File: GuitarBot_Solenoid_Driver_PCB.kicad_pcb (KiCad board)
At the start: 2 copper layers, 123.2 x 109.2 mm, 89 parts, among them J3V3 Screw_Terminal_01x02, Q1 NMOS, Q10 NMOS, Q11 NMOS, Q12 NMOS, Q13 NMOS, Q14 NMOS, Q15 NMOS, Q16 NMOS, Q2 NMOS, Q3 NMOS, Q4 NMOS, Q5 NMOS, Q6 NMOS, Q7 NMOS, Q8 NMOS, Q9 NMOS, U1 MCP23017_SP

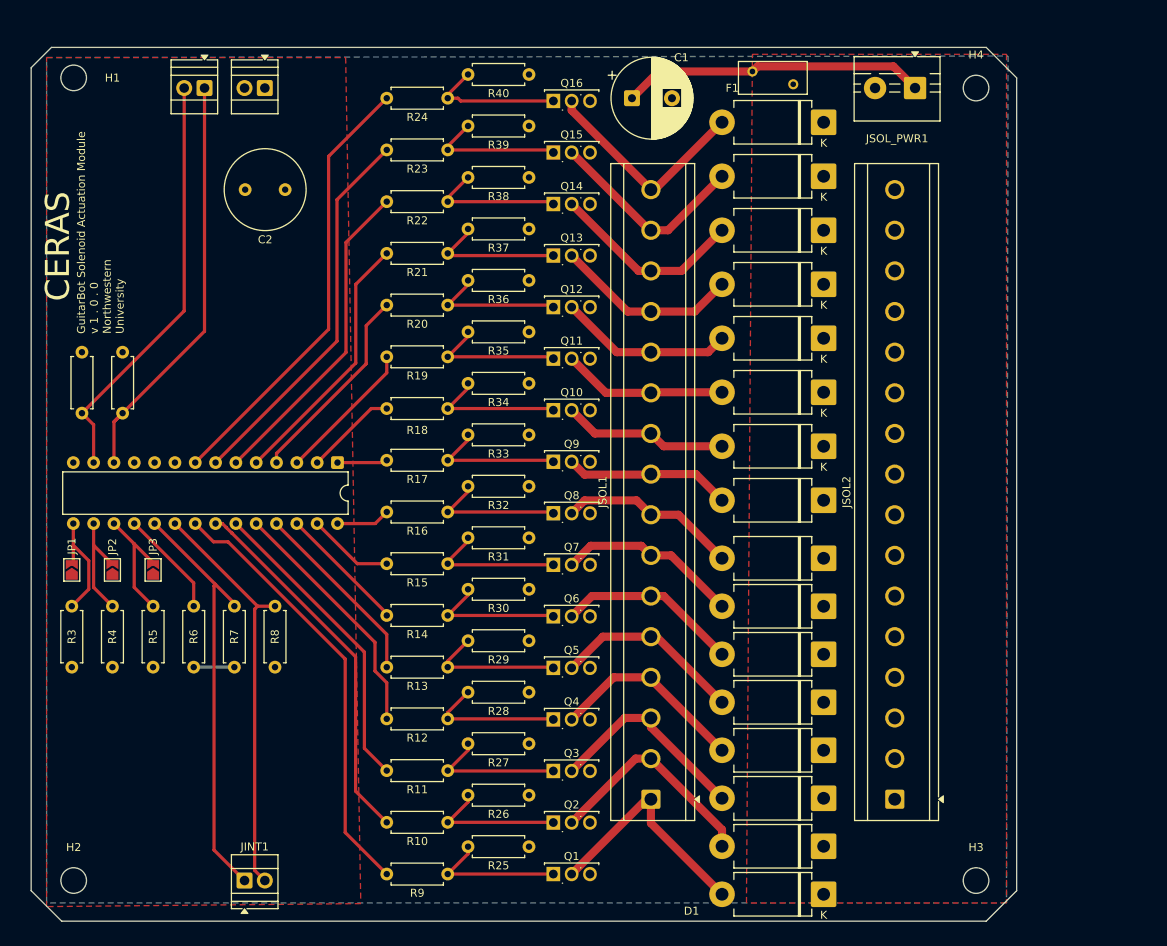
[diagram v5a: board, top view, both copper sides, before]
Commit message: Added labelling for inputs and outputs
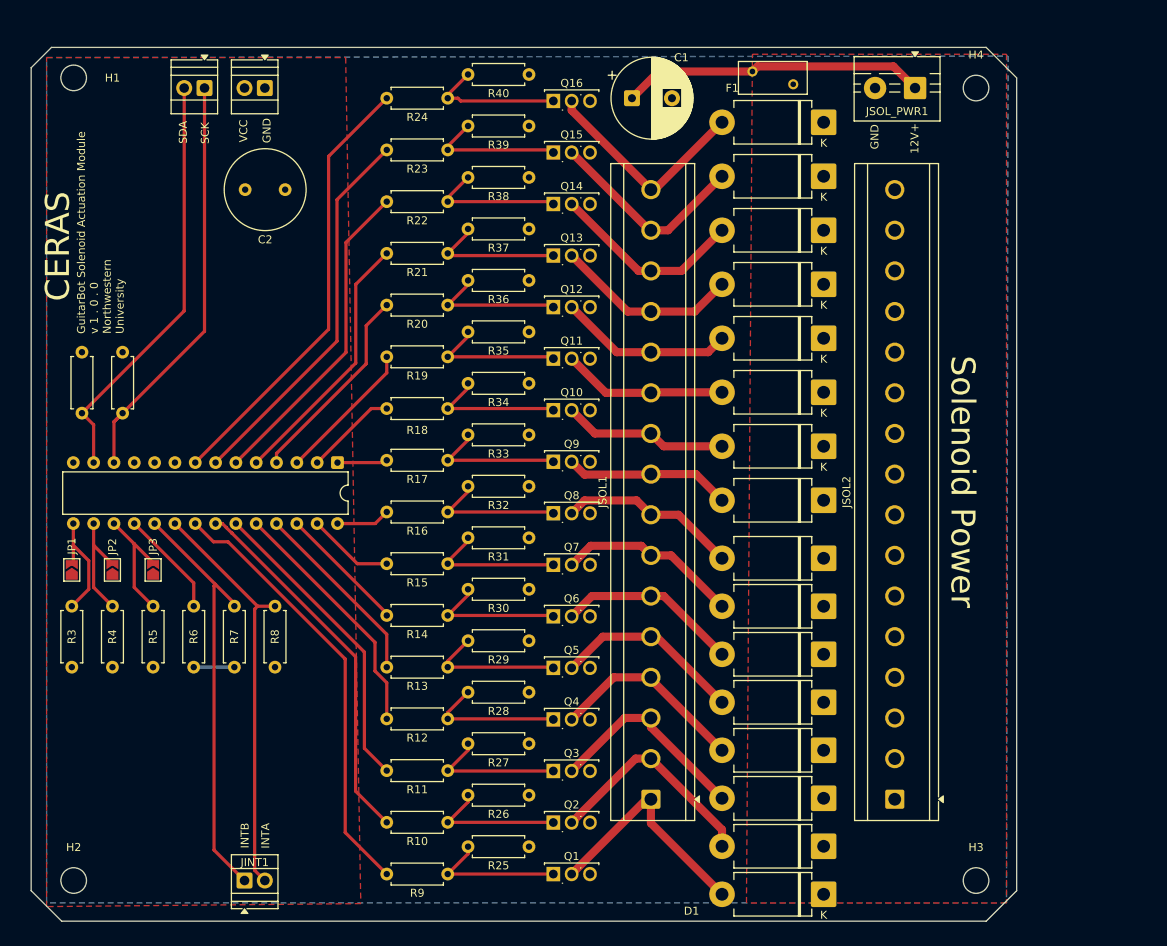
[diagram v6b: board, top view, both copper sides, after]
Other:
- board text added: "12V+"
- board text added: "GND"
- board text added: "INTA"
- board text added: "INTB"
- board text added: "SCK"
- board text added: "SDA"
- board text added: "Solenoid Power"
- board text added: "VCC"

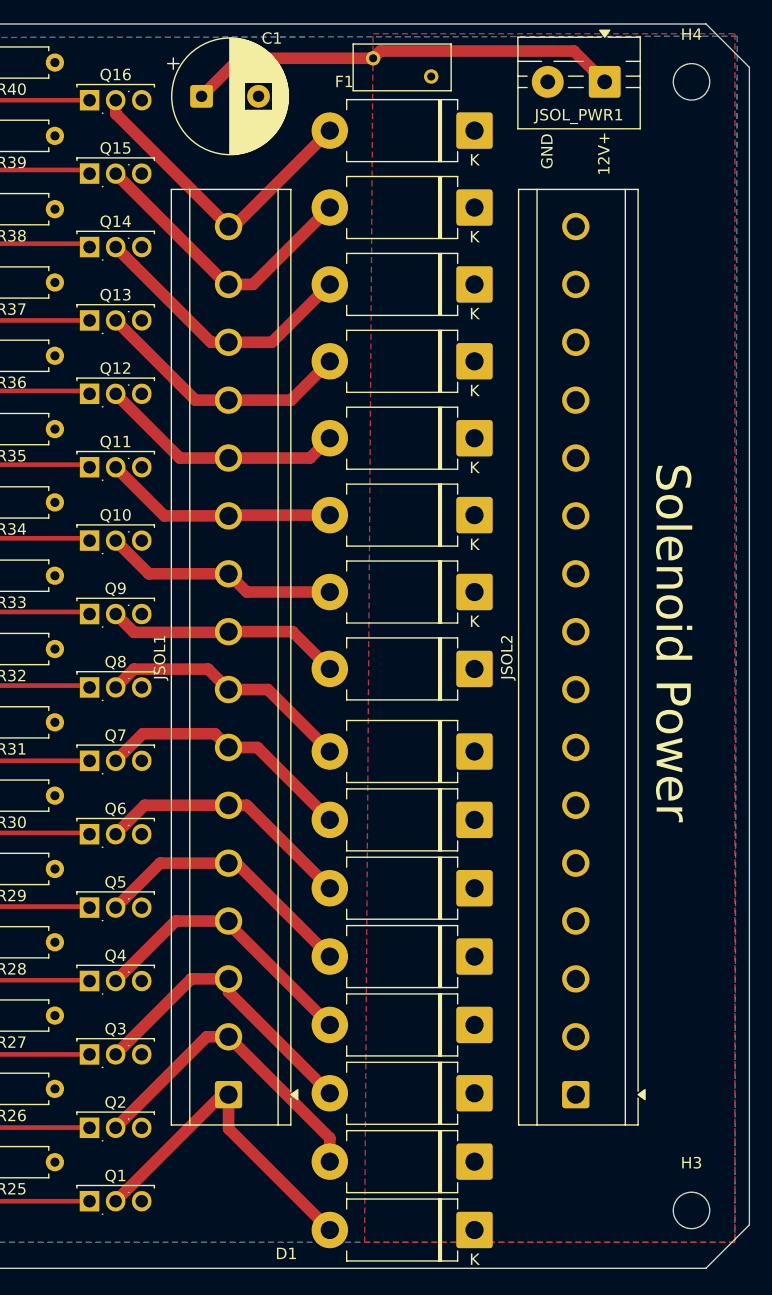
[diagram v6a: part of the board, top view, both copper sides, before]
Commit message: Reverted NMOS footprint to 220-3. Rearranged terminalblocks to fit accordingly.
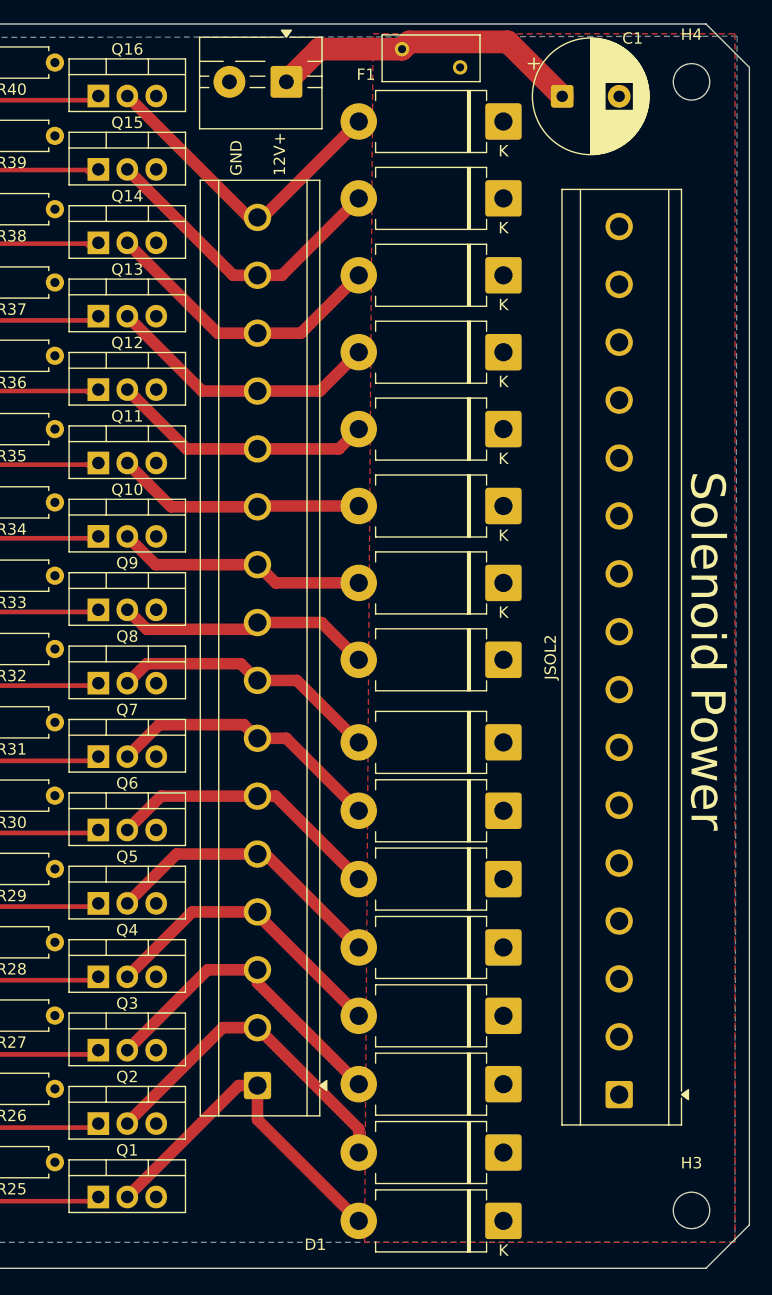
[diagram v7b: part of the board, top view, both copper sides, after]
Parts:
- Q1, Q10, Q11, Q12, Q13, Q14, Q15, Q16, Q2, Q3, Q4, Q5, Q6, Q7, Q8, Q9: footprint Package_TO_SOT_THT:TO-251-3_Vertical -> Package_TO_SOT_THT:TO-220-3_Vertical
- moved C1 31.7 mm to (158.8, 44.5)
- moved JSOL_PWR1 27.9 mm to (134.6, 43.2)
- moved JSOL2 3.81 mm to (163.8, 132.1)
- moved JSOL1 2.66 mm to (132.1, 131.3)
- moved D1 2.66 mm to (153.7, 143.2)
- moved D2 2.66 mm to (153.7, 137.2)
- moved D3 2.66 mm to (153.7, 131.2)
- moved D14 2.66 mm to (153.7, 60.2)
- moved D15 2.66 mm to (153.7, 53.4)
- moved D16 2.66 mm to (153.7, 46.7)
- moved F1 2.66 mm to (149.9, 41.9)
- moved D10 2.66 mm to (153.7, 87.2)
- moved D11 2.66 mm to (153.7, 80.4)
- moved D12 2.66 mm to (153.7, 73.7)
- moved D13 2.66 mm to (153.7, 66.9)
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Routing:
- net Net-(JSOL_PWR1-Pin_1): track 38.2 -> 27.6 mm
- net Net-(D9-A): track 20.8 -> 22.6 mm
- net Net-(D2-A): track 27.9 -> 29.6 mm
- net Net-(D5-A): track 23.8 -> 25.5 mm
- net Net-(D7-A): track 22.9 -> 24.6 mm
- net Net-(D6-A): track 22.9 -> 24.6 mm
- net Net-(D1-A): track 29.3 -> 31.0 mm
- net Net-(D4-A): track 24.9 -> 26.6 mm
- net Net-(D3-A): track 26.4 -> 28.1 mm
- net Net-(D8-A): track 22.5 -> 23.9 mm
- net Net-(D11-A): track 20.6 -> 21.9 mm
- net Net-(D12-A): track 21.9 -> 23.2 mm
- net Net-(D10-A): track 20.7 -> 22.0 mm
- net Net-(D15-A): track 25.6 -> 27.0 mm
- net Net-(D14-A): track 24.4 -> 25.7 mm
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
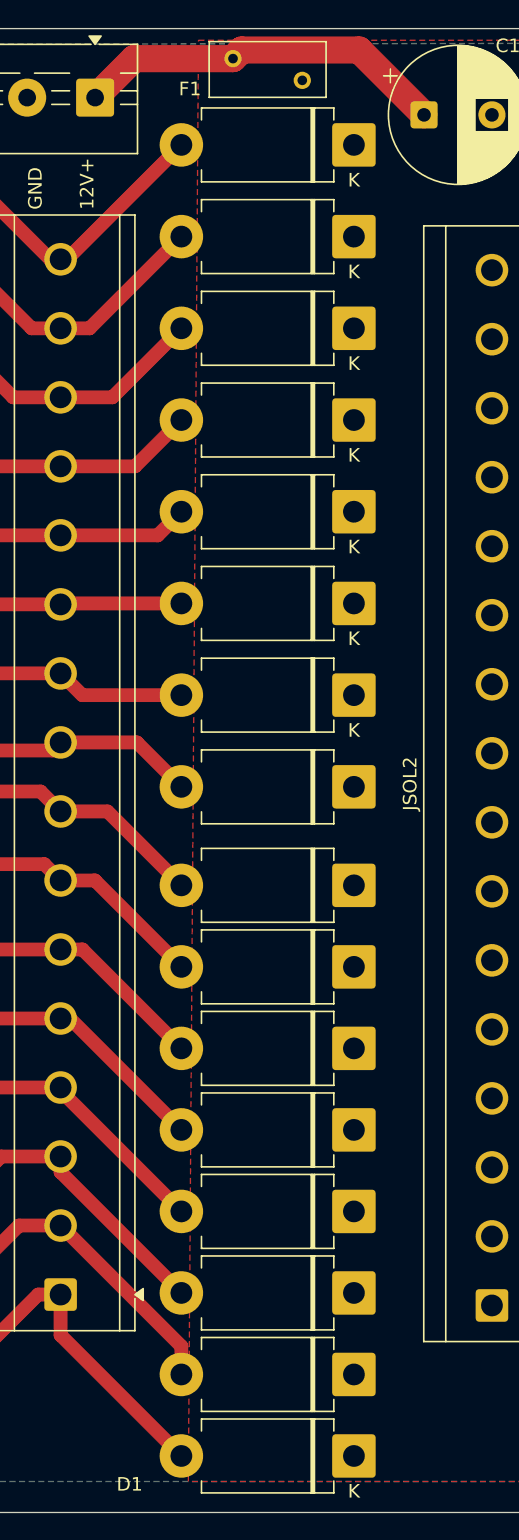
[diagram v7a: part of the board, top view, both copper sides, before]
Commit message: changed polyfuse footprint
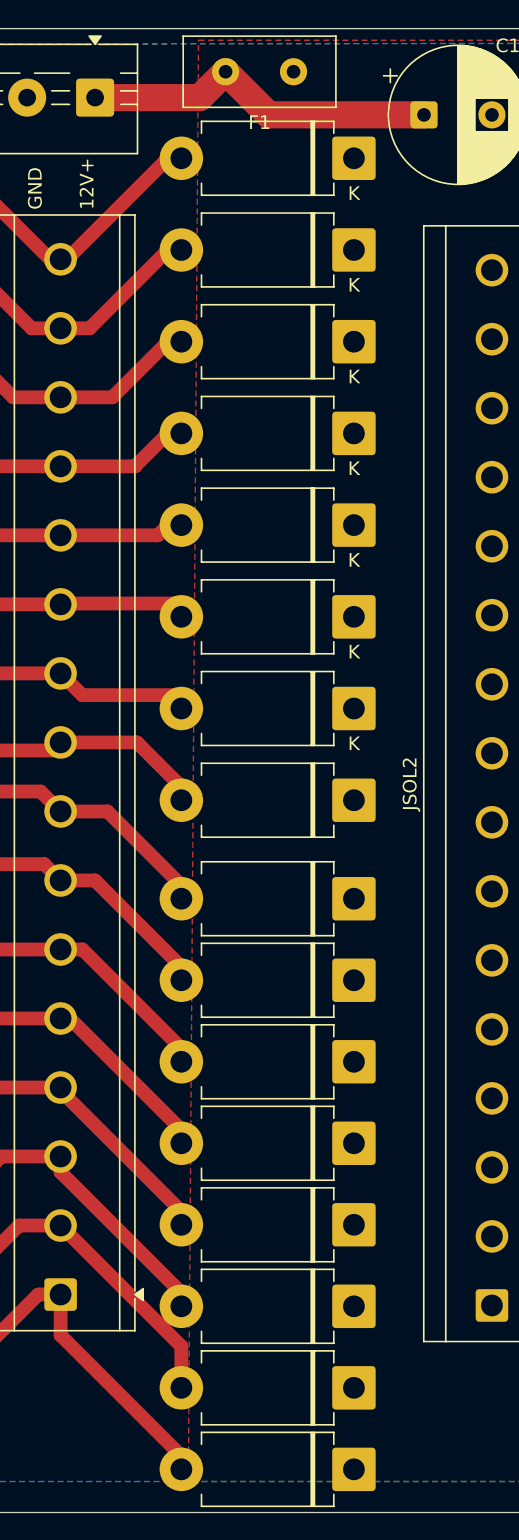
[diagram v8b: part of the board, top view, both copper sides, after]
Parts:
- F1: footprint Fuse:Fuse_BelFuse_0ZRE0005FF_L8.3mm_W3.8mm -> Capacitor_THT:C_Disc_D11.0mm_W5.0mm_P5.00mm
- moved D1 0.99 mm to (153.7, 144.1)
- moved D2 0.99 mm to (153.7, 138.1)
- moved D3 0.99 mm to (153.7, 132.1)
- moved D14 0.99 mm to (153.7, 61.1)
- moved D15 0.99 mm to (153.7, 54.4)
- moved D16 0.99 mm to (153.7, 47.6)
- moved D10 0.98 mm to (153.7, 88.1)
- moved D11 0.98 mm to (153.7, 81.4)
- moved D12 0.98 mm to (153.7, 74.6)
- moved D13 0.98 mm to (153.7, 67.9)
- moved D4 0.98 mm to (153.7, 126.1)
- moved D5 0.98 mm to (153.7, 120.1)
- moved D6 0.98 mm to (153.7, 114.1)
- moved D7 0.98 mm to (153.7, 108.1)
- moved D8 0.98 mm to (153.7, 102.1)
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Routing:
- net Net-(JSOL_PWR1-Pin_1): track 27.6 -> 26.3 mm
